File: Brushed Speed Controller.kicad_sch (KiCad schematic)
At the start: 4 parts, among them Q1 ISC037N03L5ISATMA1, Q2 ISC037N03L5ISATMA1, Q3 BSC340N08NS3, Q4 BSC340N08NS3

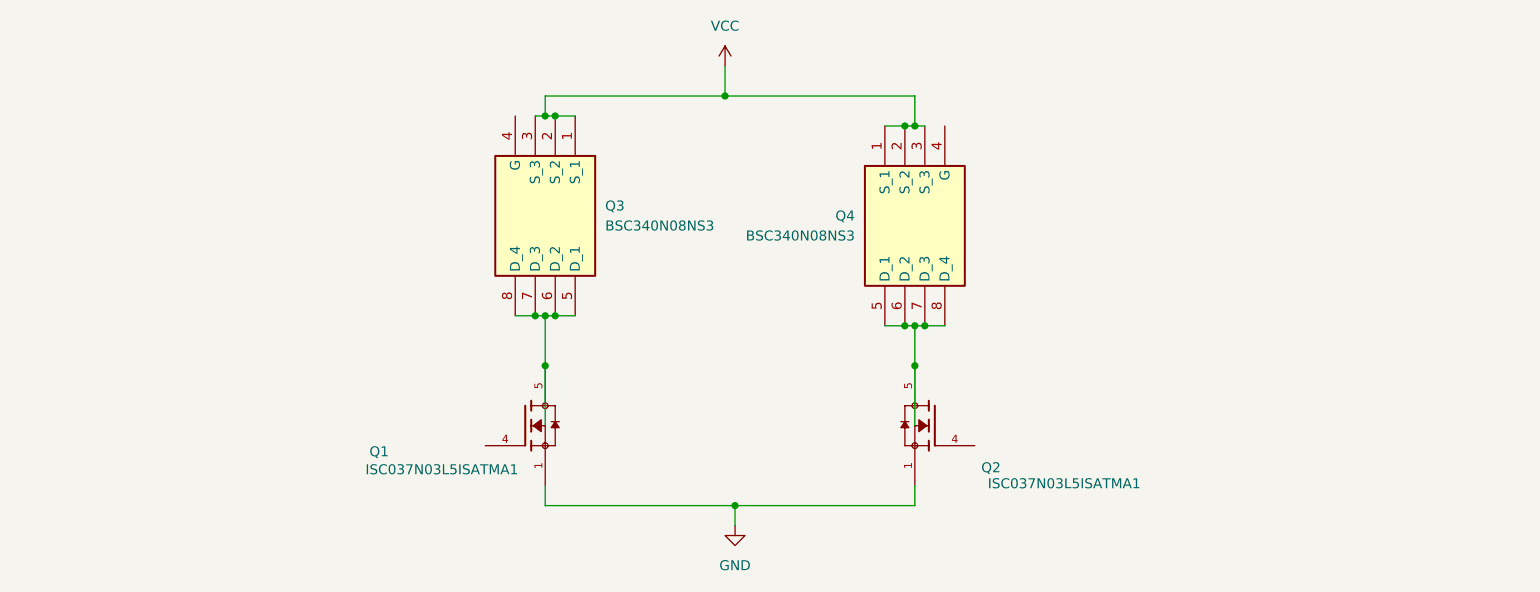
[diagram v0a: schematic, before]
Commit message: added mosfet Driver
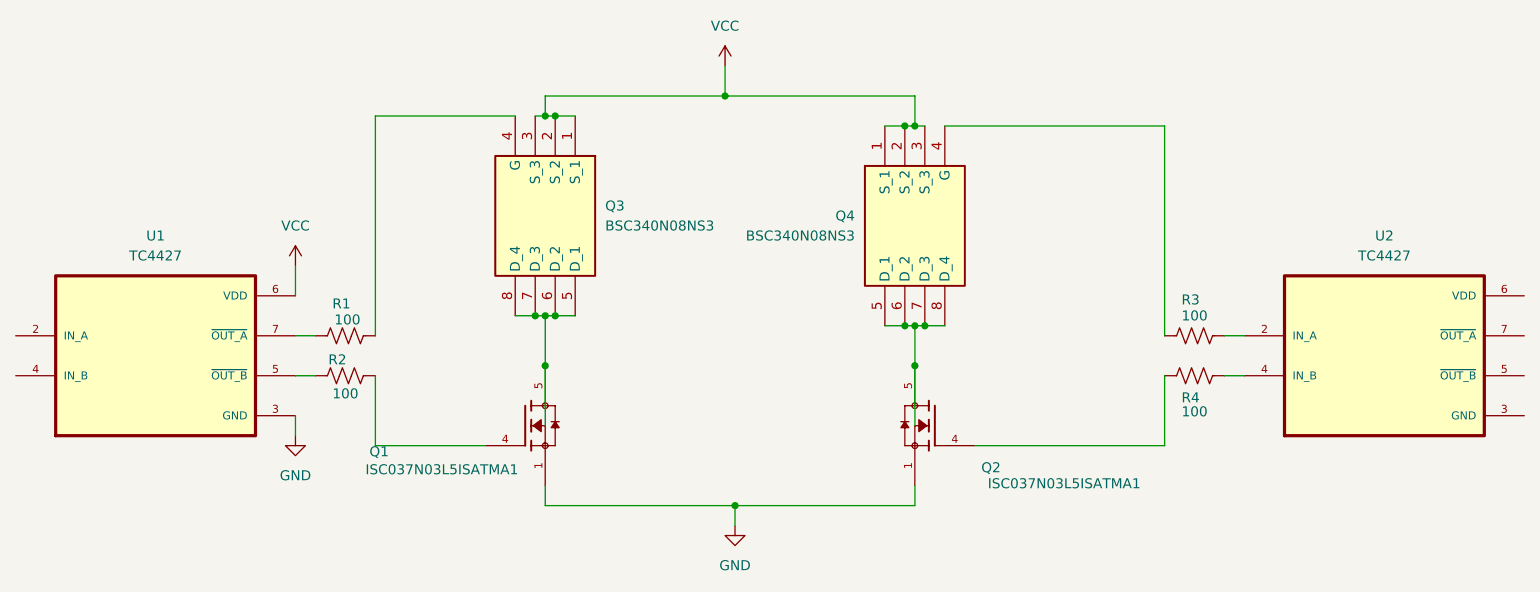
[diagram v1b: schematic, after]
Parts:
- added R1, R2, R3, R4: 100, symbol Device:R_US
- added U1, U2: TC4427, TC4427:TC4427, symbol TC4427:TC4427
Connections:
- net GND: now also U1.3 (GND)
- net VCC: now also U1.6 (VDD)
- net at Q4.4 (G): now also R3.1
- net at Q3.4 (G): now also R1.2
- net at Q2.4: now also R4.1
- net at Q1.4: now also R2.2
- new net: R4.2, U2.4 (IN_B)
- new net: R2.1, U1.5 (~{OUT_B})
- new net: R1.1, U1.7 (~{OUT_A})
- new net: R3.2, U2.2 (IN_A)

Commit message: fixed symbol load issue
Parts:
- Q1, Q2: footprint ISC037N03L5ISATMA1:IC_ISC037N03L5ISATMA1 -> ISC037N03:IC_ISC037N03L5ISATMA1
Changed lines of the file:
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@@
 			)
 		)
-		(property "Footprint" "ISC037N03L5ISATMA1:IC_ISC037N03L5ISATMA1"
+		(property "Footprint" "ISC037N03:IC_ISC037N03L5ISATMA1"
 			(at 158.75 81.28 0)
 			(effects
@@
 			)
 		)
-		(property "Footprint" "ISC037N03L5ISATMA1:IC_ISC037N03L5ISATMA1"
+		(property "Footprint" "ISC037N03:IC_ISC037N03L5ISATMA1"
 			(at 106.68 81.28 0)
 			(effects

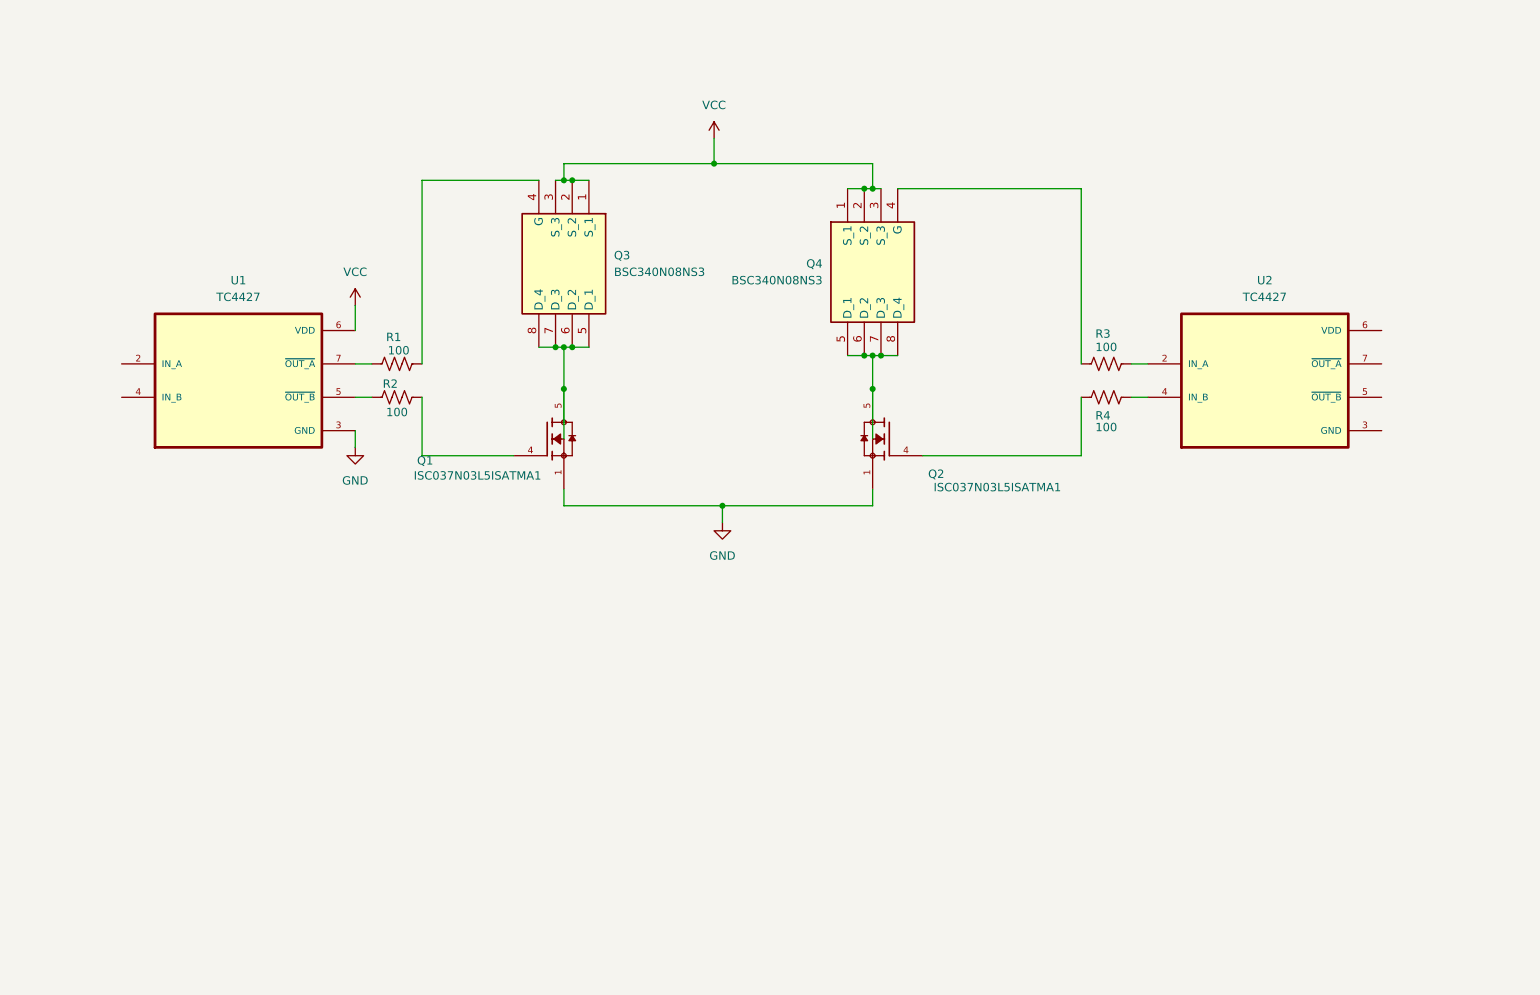
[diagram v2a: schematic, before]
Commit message: Made first prototype PCB
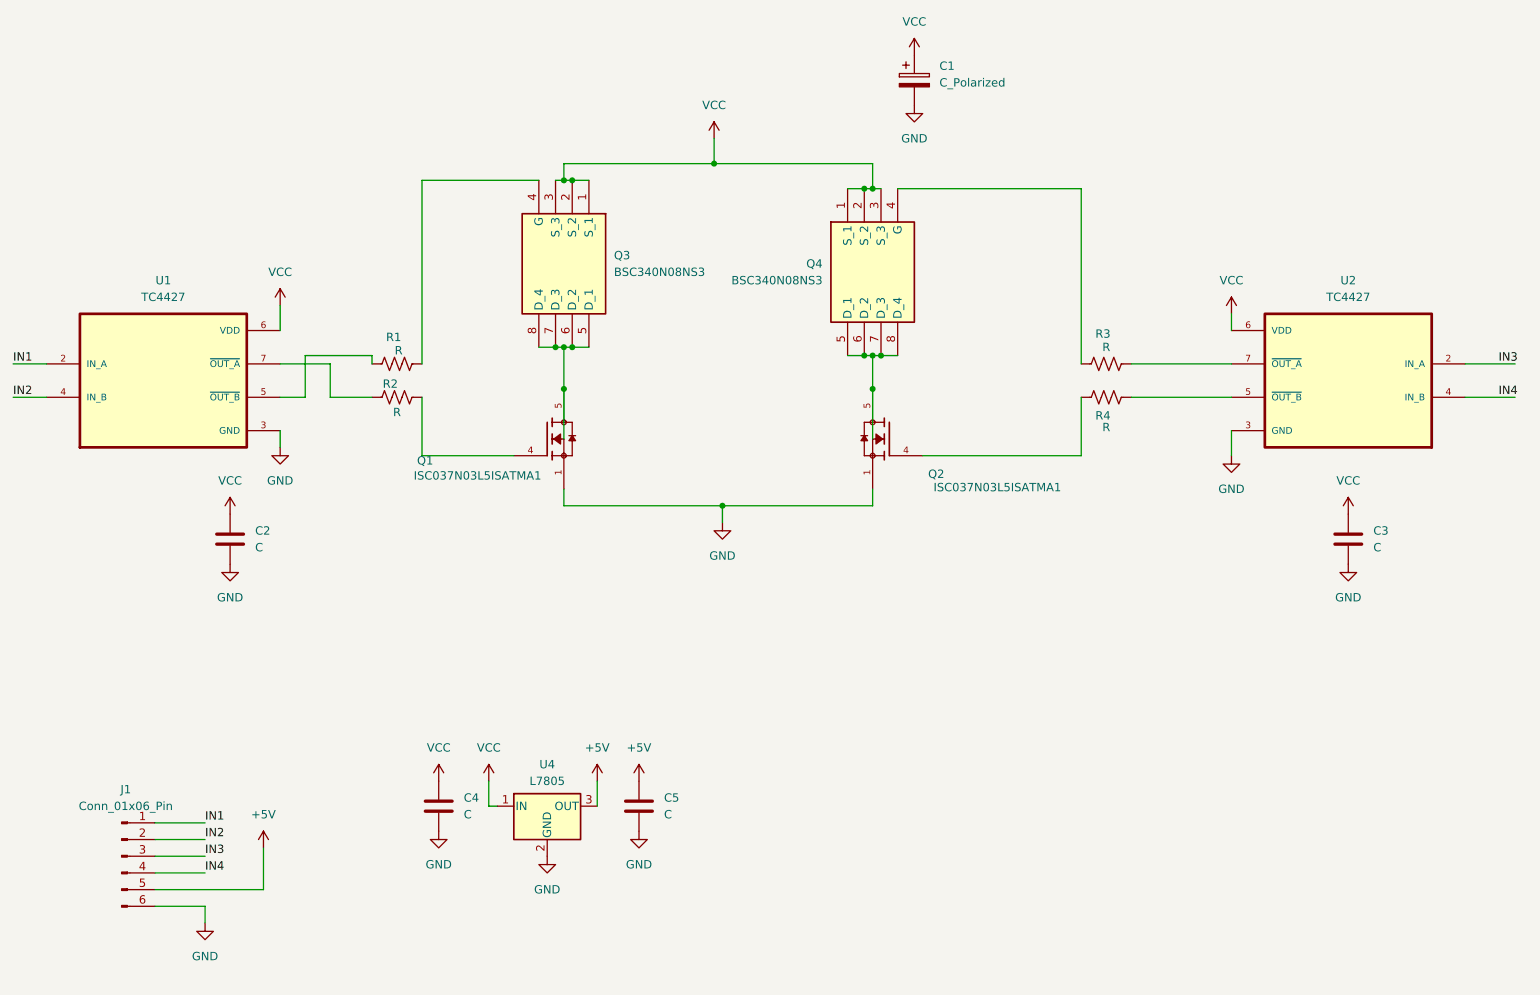
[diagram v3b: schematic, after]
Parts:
- added C1: C_Polarized, Capacitor_THT:CP_Radial_D8.0mm_P5.00mm, symbol Device:C_Polarized
- added C2, C3, C4, C5: C, Capacitor_THT:CP_Radial_D8.0mm_P5.00mm, symbol Device:C
- added J1: Conn_01x06_Pin, Connector_PinHeader_2.00mm:PinHeader_1x06_P2.00mm_Vertical, symbol Connector:Conn_01x06_Pin
- added U4: L7805, Package_TO_SOT_THT:TO-220-3_Vertical, symbol Regulator_Linear:L7805
- R1, R2, R3, R4: value 100 -> R; footprint (none) -> Resistor_THT:R_Axial_DIN0207_L6.3mm_D2.5mm_P10.16mm_Horizontal
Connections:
- net GND: now also U2.3 (GND), C1.2, C2.2, C3.2, C4.2, C5.2, J1.6 (Pin_6), U4.2 (GND)
- net VCC: now also U2.6 (VDD), C1.1, C2.1, C3.1, C4.1, U4.1 (IN)
- net at R4.2: now also U2.5 (~{OUT_B}); no longer U2.4 (IN_B)
- net at R2.1: now also U1.7 (~{OUT_A}); no longer U1.5 (~{OUT_B})
- net IN1: now reaches U1.2 (IN_A)
- net IN1: now also J1.1 (Pin_1)
- net IN2: now reaches U1.4 (IN_B)
- net IN2: now also J1.2 (Pin_2)
- net at R1.1: now also U1.5 (~{OUT_B}); no longer U1.7 (~{OUT_A})
- net at R3.2: now also U2.7 (~{OUT_A}); no longer U2.2 (IN_A)
- new net +5V: C5.1, J1.5 (Pin_5), U4.3 (OUT)
- new net IN3: J1.3 (Pin_3), U2.2 (IN_A)
- new net IN4: J1.4 (Pin_4), U2.4 (IN_B)
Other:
- moved on the sheet: U1, U2

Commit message: made symbol for mosfet
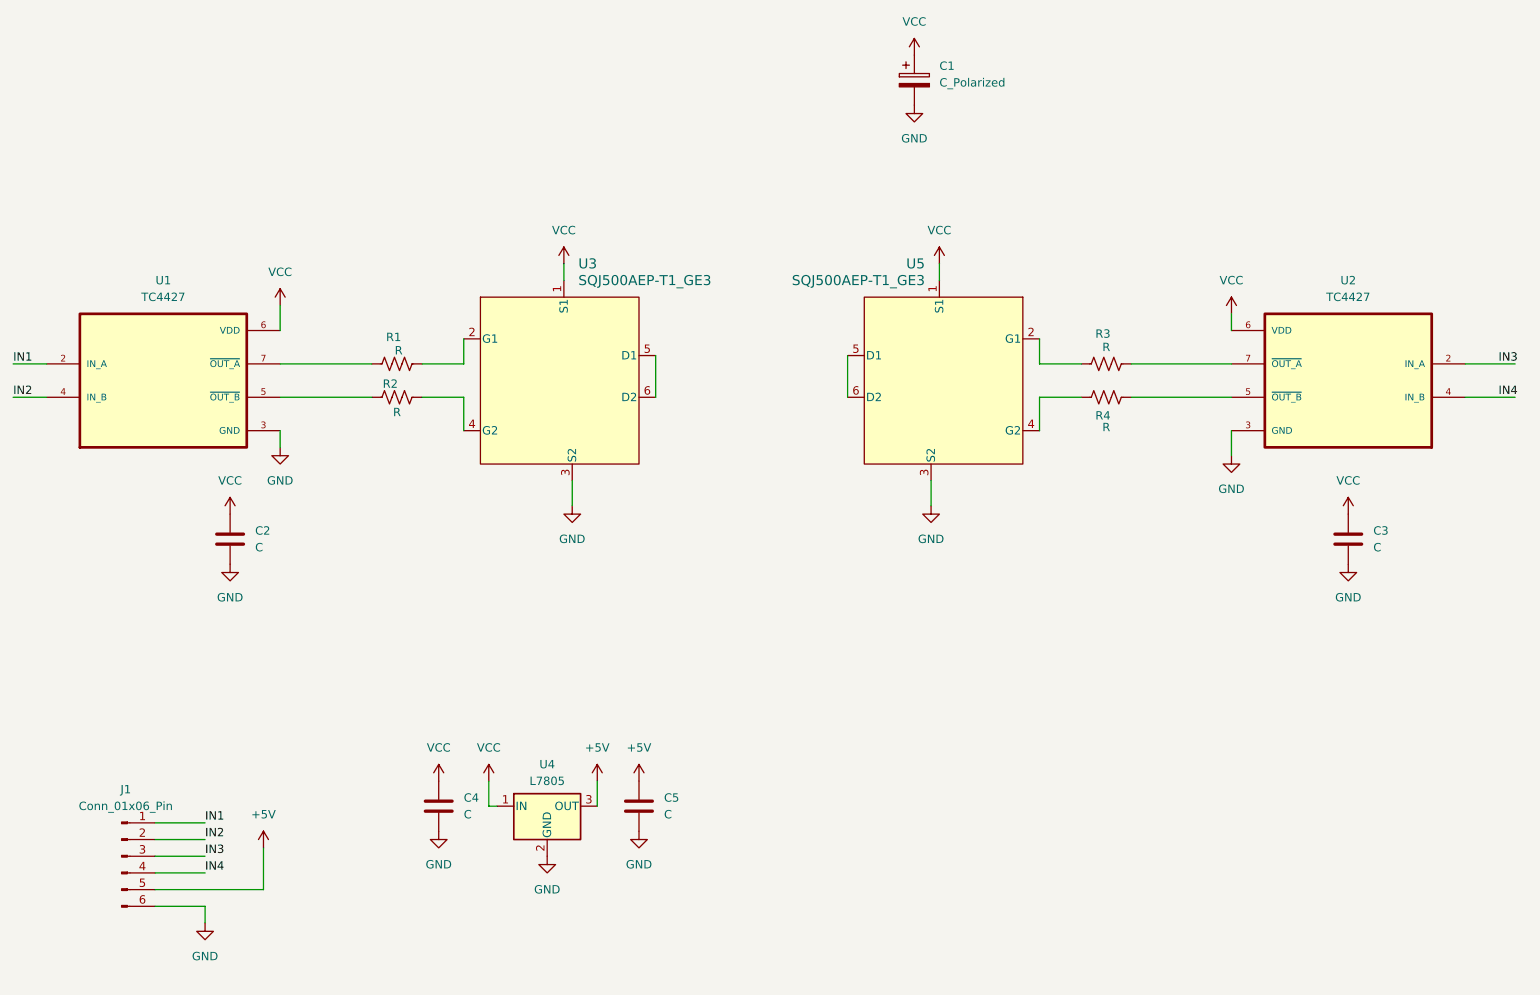
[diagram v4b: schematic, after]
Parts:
- removed Q1, Q2: ISC037N03L5ISATMA1, ISC037N03:IC_ISC037N03L5ISATMA1, symbol ISC037N03:ISC037N03L5ISATMA1
- removed Q3, Q4: BSC340N08NS3, BSC340N08:BSC340N08NS3, symbol BSC340N08:BSC340N08NS3_G
- added U3, U5: SQJ500AEP-T1_GE3, SQJ500AEP-T1-GE3:SQJ500AEP-T1-GE3, symbol SQJ500AEP-T1-GE3:SQJ500AEP-T1_GE3
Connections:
- net GND: now also U3.3 (S2), U5.3 (S2)
- net VCC: now also U3.1 (S1), U5.1 (S1)
- net at R4.1: now also U5.4 (G2)
- net at R2.1: now also U1.5 (~{OUT_B}); no longer U1.7 (~{OUT_A})
- net at R2.2: now also U3.4 (G2)
- net at R1.1: now also U1.7 (~{OUT_A}); no longer U1.5 (~{OUT_B})
- net at R3.1: now also U5.2 (G1)
- net at R1.2: now also U3.2 (G1)
- new net: U5.5 (D1), U5.6 (D2)
- new net: U3.5 (D1), U3.6 (D2)

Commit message: Completed the PCB and Schemetic
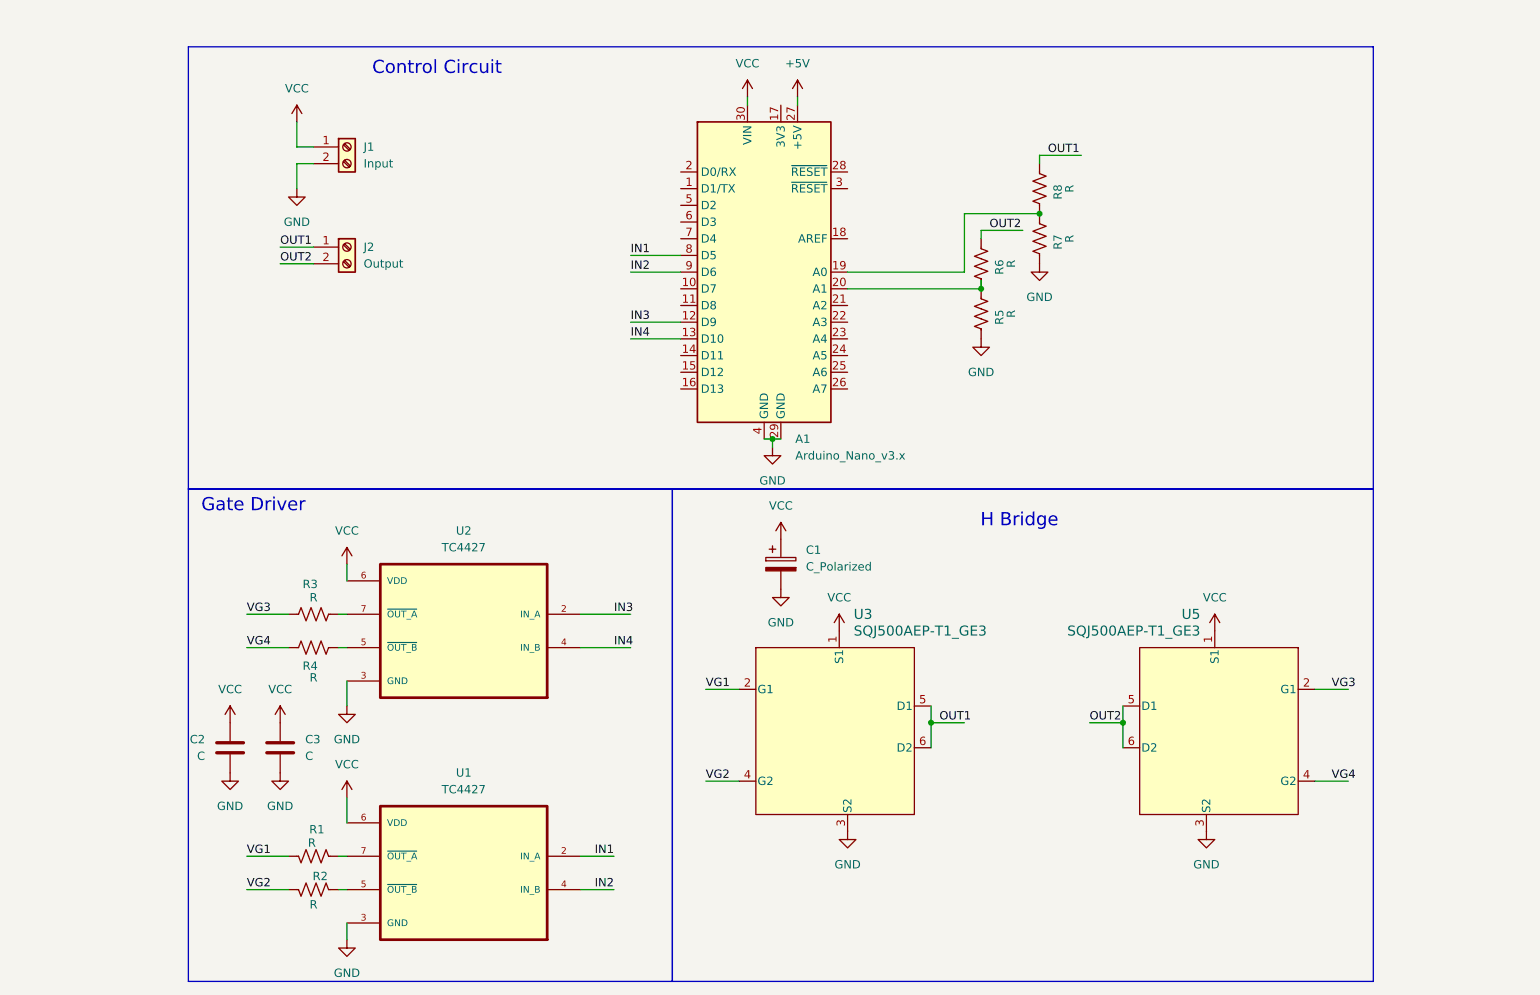
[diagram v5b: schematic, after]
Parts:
- removed C4, C5: C, Capacitor_THT:CP_Radial_D8.0mm_P5.00mm, symbol Device:C
- removed J1: Conn_01x06_Pin, Connector_PinHeader_2.00mm:PinHeader_1x06_P2.00mm_Vertical, symbol Connector:Conn_01x06_Pin
- removed U4: L7805, Package_TO_SOT_THT:TO-220-3_Vertical, symbol Regulator_Linear:L7805
- added A1: Arduino_Nano_v3.x, Module:Arduino_Nano, symbol MCU_Module:Arduino_Nano_v3.x
- added J1: Input, TerminalBlock_4Ucon:TerminalBlock_4Ucon_1x02_P3.50mm_Vertical, symbol Connector:Screw_Terminal_01x02
- added J2: Output, TerminalBlock_4Ucon:TerminalBlock_4Ucon_1x02_P3.50mm_Vertical, symbol Connector:Screw_Terminal_01x02
- added R5, R6, R7, R8: R, Resistor_THT:R_Axial_DIN0207_L6.3mm_D2.5mm_P10.16mm_Horizontal, symbol Device:R_US
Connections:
- net +5V: now also A1.27 (+5V)
- net GND: now also A1.29 (GND), A1.4 (GND), J1.2 (Pin_2), R5.1, R7.1
- net IN1: now also A1.8 (D5)
- net IN2: now also A1.9 (D6)
- net IN3: now also A1.12 (D9)
- net IN4: now also A1.13 (D10)
- net VCC: now also A1.30 (VIN), J1.1 (Pin_1)
- net VG4: now reaches R4.1, U5.4 (G2)
- net VG2: now reaches R2.2, U3.4 (G2)
- net VG1: now reaches R1.2, U3.2 (G1)
- net VG3: now reaches R3.1, U5.2 (G1)
- net OUT2: now reaches U5.5 (D1), U5.6 (D2)
- net OUT2: now also J2.2 (Pin_2), R6.2
- net OUT1: now reaches U3.5 (D1), U3.6 (D2)
- net OUT1: now also J2.1 (Pin_1), R8.2
- new net: A1.20 (A1), R5.2, R6.1
- new net: A1.19 (A0), R7.2, R8.1
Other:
- note added: "Control Circuit"
- note added: "Gate Driver"
- note added: "H Bridge"
- moved on the sheet: C1, C2, C3, R1, R2, R3, R4, U1, U2, U3, U5
